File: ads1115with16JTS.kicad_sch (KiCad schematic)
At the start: 48 parts, among them J1 Conn_01x02_Pin, J10 Conn_01x02_Pin, J11 Conn_01x02_Pin, J12 Conn_01x02_Pin, J13 Conn_01x02_Pin, J14 Conn_01x02_Pin, J15 Conn_01x02_Pin, J16 Conn_01x02_Pin, J17 Conn_01x04_Pin, J18 PinSocket_1x20_P2.54mm_Vertic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, J19 PinSocket_1x20_P2.54mm_Vertic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, J2 Conn_01x02_Pin, J3 Conn_01x02_Pin, J4 Conn_01x02_Pin, J5 Conn_01x02_Pin, J6 Conn_01x02_Pin, J7 Conn_01x02_Pin, J8 Conn_01x02_Pin, J9 Conn_01x02_Pin, U1 ADS1115IDGS, U2 ADS1115IDGS, U3 ADS1115IDGS, U4 ADS1115IDGS

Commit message: snapshot v0.1.0-pre
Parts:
- removed pads1: SolderWire-0.25sqmm_1x04_P4.2mm_D0.65mm_OD1.7mm, SolderWire-0.25sqmm_1x04_P4.2mm_D0.65mm_OD1.7mm, symbol Connector:Conn_01x04_Pin
- added J20: Screw_Terminal_01x02, TerminalBlock_Phoenix:TerminalBlock_Phoenix_MPT-0,5-2-2.54_1x02_P2.54mm_Horizontal, symbol Connector:Screw_Terminal_01x02
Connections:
- net +3V3: now also J20.2 (Pin_2)
- net GND: now also J20.1 (Pin_1)
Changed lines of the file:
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@@
   (junction (at 125.73 171.45) (diameter 0) (color 0 0 0 0)
   )
-  (junction (at 184.15 53.34) (diameter 0) (color 0 0 0 0)
-  )
   (junction (at 125.73 142.24) (diameter 0) (color 0 0 0 0)
   )
@@
   (junction (at 186.69 105.41) (diameter 0) (color 0 0 0 0)
   )
-  (junction (at 186.69 50.8) (diameter 0) (color 0 0 0 0)
-  )
   (junction (at 143.51 69.85) (diameter 0) (color 0 0 0 0)
   )
-  (junction (at 193.04 58.42) (diameter 0) (color 0 0 0 0)
-  )
   (junction (at 190.5 113.03) (diameter 0) (color 0 0 0 0)
   )
@@
   (junction (at 48.26 184.15) (diameter 0) (color 0 0 0 0)
   )
-  (junction (at 190.5 55.88) (diameter 0) (color 0 0 0 0)
+  (junction (at 186.69 78.74) (diameter 0) (color 0 0 0 0)
   )
   (junction (at 162.56 148.59) (diameter 0) (color 0 0 0 0)
@@
   )
   (junction (at 189.23 110.49) (diameter 0) (color 0 0 0 0)
+  )
+  (junction (at 184.15 81.28) (diameter 0) (color 0 0 0 0)
   )
   (junction (at 49.53 250.19) (diameter 0) (color 0 0 0 0)
@@
     (stroke (width 0) (type default))
   )
-  (wire (pts (xy 189.23 55.88) (xy 190.5 55.88))
+  (wire (pts (xy 189.23 55.88) (xy 194.31 55.88))
     (stroke (width 0) (type default))
   )
@@
     (stroke (width 0) (type default))
   )
-  (wire (pts (xy 190.5 55.88) (xy 194.31 55.88))
-    (stroke (width 0) (type default))
-  )
   (wire (pts (xy 182.88 148.59) (xy 191.77 148.59))
     (stroke (width 0) (type default))
@@
     (stroke (width 0) (type default))
   )
+  (wire (pts (xy 186.69 78.74) (xy 186.69 62.23))
+    (stroke (width 0) (type default))
+  )
   (wire (pts (xy 140.97 218.44) (xy 138.43 218.44))
     (stroke (width 0) (type default))
@@
     (stroke (width 0) (type default))
   )
-  (wire (pts (xy 193.04 58.42) (xy 194.31 58.42))
+  (wire (pts (xy 190.5 58.42) (xy 194.31 58.42))
     (stroke (width 0) (type default))
   )
@@
     (stroke (width 0) (type default))
   )
-  (wire (pts (xy 190.5 38.1) (xy 190.5 55.88))
-    (stroke (width 0) (type default))
-  )
   (wire (pts (xy 182.88 123.19) (xy 191.77 123.19))
     (stroke (width 0) (type default))
@@
     (stroke (width 0) (type default))
   )
-  (wire (pts (xy 193.04 40.64) (xy 193.04 58.42))
-    (stroke (width 0) (type default))
-  )
   (wire (pts (xy 105.41 45.72) (xy 115.57 45.72))
     (stroke (width 0) (type default))
@@
     (stroke (width 0) (type default))
   )
+  (wire (pts (xy 184.15 81.28) (xy 184.15 64.77))
+    (stroke (width 0) (type default))
+  )
   (wire (pts (xy 186.69 50.8) (xy 194.31 50.8))
     (stroke (width 0) (type default))
   )
-  (wire (pts (xy 184.15 35.56) (xy 184.15 53.34))
-    (stroke (width 0) (type default))
-  )
   (wire (pts (xy 182.88 113.03) (xy 190.5 113.03))
     (stroke (width 0) (type default))
@@
     (stroke (width 0) (type default))
   )
+  (wire (pts (xy 175.26 78.74) (xy 186.69 78.74))
+    (stroke (width 0) (type default))
+  )
   (wire (pts (xy 78.74 148.59) (xy 115.57 148.59))
     (stroke (width 0) (type default))
@@
     (stroke (width 0) (type default))
   )
-  (wire (pts (xy 184.15 102.87) (xy 184.15 64.77))
+  (wire (pts (xy 184.15 102.87) (xy 184.15 81.28))
     (stroke (width 0) (type default))
   )
@@
     (stroke (width 0) (type default))
   )
-  (wire (pts (xy 190.5 58.42) (xy 193.04 58.42))
-    (stroke (width 0) (type default))
-  )
   (wire (pts (xy 157.48 120.65) (xy 162.56 120.65))
     (stroke (width 0) (type default))
@@
     (stroke (width 0) (type default))
   )
+  (wire (pts (xy 175.26 81.28) (xy 184.15 81.28))
+    (stroke (width 0) (type default))
+  )
   (wire (pts (xy 143.51 69.85) (xy 143.51 104.14))
     (stroke (width 0) (type default))
@@
     (stroke (width 0) (type default))
   )
-  (wire (pts (xy 193.04 38.1) (xy 190.5 38.1))
-    (stroke (width 0) (type default))
-  )
   (wire (pts (xy 157.48 151.13) (xy 162.56 151.13))
     (stroke (width 0) (type default))
@@
     (stroke (width 0) (type default))
   )
-  (wire (pts (xy 186.69 33.02) (xy 186.69 50.8))
-    (stroke (width 0) (type default))
-  )
   (wire (pts (xy 182.88 140.97) (xy 191.77 140.97))
     (stroke (width 0) (type default))
@@
     (stroke (width 0) (type default))
   )
-  (wire (pts (xy 193.04 33.02) (xy 186.69 33.02))
-    (stroke (width 0) (type default))
-  )
   (wire (pts (xy 160.02 64.77) (xy 167.64 64.77))
     (stroke (width 0) (type default))
@@
     (stroke (width 0) (type default))
   )
-  (wire (pts (xy 193.04 35.56) (xy 184.15 35.56))
-    (stroke (width 0) (type default))
-  )
-  (wire (pts (xy 186.69 105.41) (xy 186.69 62.23))
+  (wire (pts (xy 186.69 105.41) (xy 186.69 78.74))
     (stroke (width 0) (type default))
   )
@@
     )
   )
-  (symbol (lib_id "Connector:Conn_01x04_Pin") (at 198.12 35.56 0) (mirror y) (unit 1)
-    (in_bom yes) (on_board yes) (dnp no)
-    (property "Reference" "pads1" (at 197.485 27.94 0)
-      (effects (font (size 1.27 1.27)))
-    )
-    (property "Value" "SolderWire-0.25sqmm_1x04_P4.2mm_D0.65mm_OD1.7mm\n" (at 197.485 30.48 0)
-      (effects (font (size 1.27 1.27)))
-    )
-    (property "Footprint" "SolderWire-0.25sqmm_1x04_P4.2mm_D0.65mm_OD1.7mm" (at 198.12 35.56 0)
-      (effects (font (size 1.27 1.27)) hide)
-    )
-    (property "Datasheet" "~" (at 198.12 35.56 0)
-      (effects (font (size 1.27 1.27)) hide)
-    )
-    (pin "1")
-    (pin "2")
-    (pin "3")
-    (pin "4")
-    (instances
-      (project "ads1115with16JTS"
-        (path "/0c2d0c14-8850-4a30-bb78-b2f40cb442ba"
-          (reference "pads1") (unit 1)
-        )
-      )
-    )
-  )
   (symbol (lib_id "power:+3V3") (at 48.26 31.75 0) (unit 1)
     (in_bom yes) (on_board yes) (dnp no)
@@
         )
       )
+    )
+  )
+  (symbol (lib_id "Connector:Screw_Terminal_01x02") (at 170.18 78.74 0) (mirror y) (unit 1)
+    (in_bom yes) (on_board yes) (dnp no)
+    (property "Reference" "J20" (at 167.64 78.74 0)
+      (effects (font (size 1.27 1.27)) (justify left))
+    )
+    (property "Value" "Screw_Terminal_01x02" (at 167.64 81.28 0)
+      (effects (font (size 1.27 1.27)) (justify left))
+    )
+    (property "Footprint" "TerminalBlock_Phoenix:TerminalBlock_Phoenix_MPT-0,5-2-2.54_1x02_P2.54mm_Horizontal" (at 170.18 78.74 0)
+      (effects (font (size 1.27 1.27)) hide)
+    )
+    (property "Datasheet" "~" (at 170.18 78.74 0)
+      (effects (font (size 1.27 1.27)) hide)
+    )
+    (pin "1")
+    (pin "2")
+    (instances
+      (project "ads1115with16JTS"
+        (path "/0c2d0c14-8850-4a30-bb78-b2f40cb442ba"
+          (reference "J20") (unit 1)
+        )
+      )

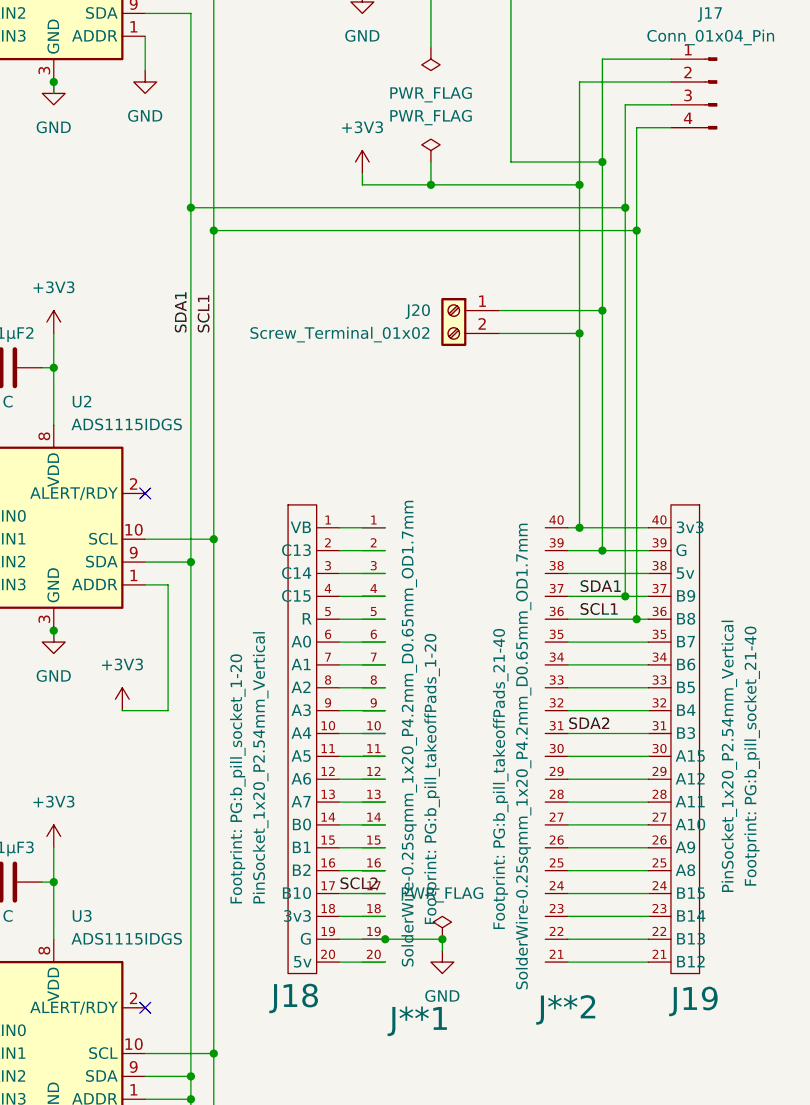
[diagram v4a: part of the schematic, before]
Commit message: change solder mask for takeoff pads, which will not be soldered.
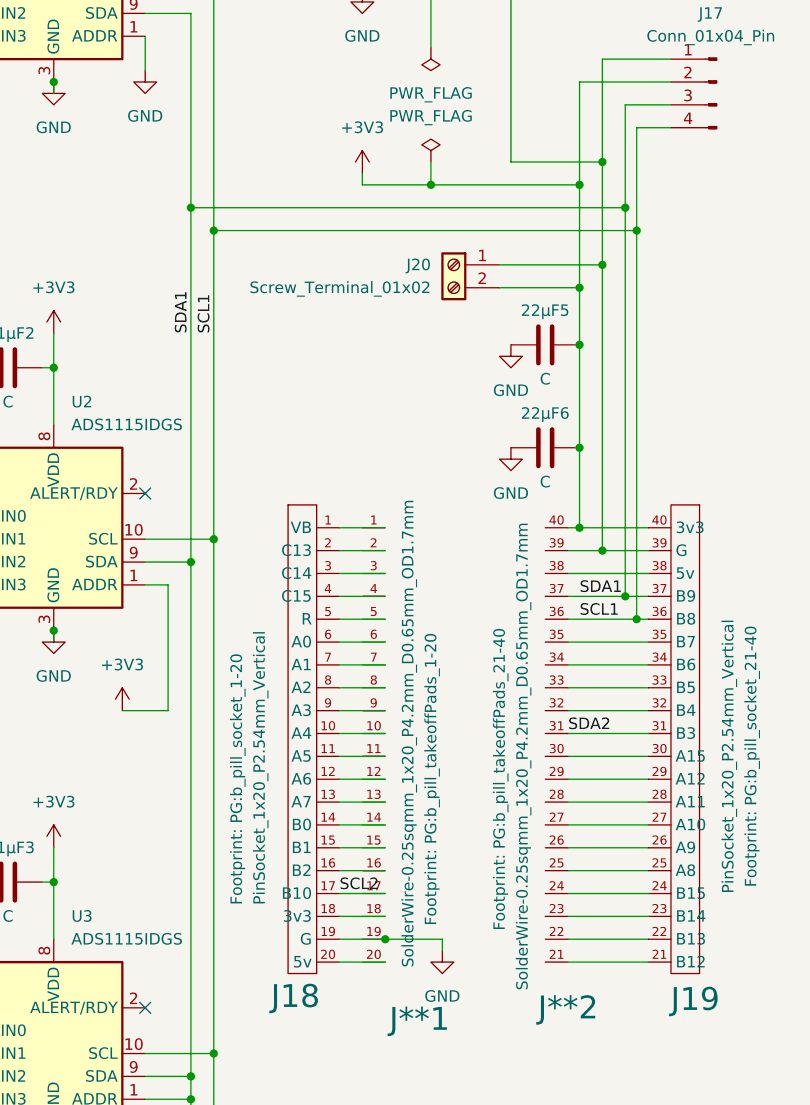
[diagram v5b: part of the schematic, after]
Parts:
- added 22µF5, 22µF6: C, Capacitor_SMD:C_0805_2012Metric, symbol Device:C
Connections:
- net +3V3: now also 22µF5.1, 22µF6.1
- net GND: now also 22µF5.2, 22µF6.2
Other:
- moved on the sheet: J20
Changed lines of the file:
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@@
   (junction (at 184.15 102.87) (diameter 0) (color 0 0 0 0)
   )
+  (junction (at 186.69 73.66) (diameter 0) (color 0 0 0 0)
+  )
   (junction (at 140.97 166.37) (diameter 0) (color 0 0 0 0)
   )
@@
   (junction (at 140.97 67.31) (diameter 0) (color 0 0 0 0)
   )
-  (junction (at 168.91 148.59) (diameter 0) (color 0 0 0 0)
-  )
   (junction (at 125.73 171.45) (diameter 0) (color 0 0 0 0)
   )
@@
   (junction (at 143.51 69.85) (diameter 0) (color 0 0 0 0)
   )
+  (junction (at 184.15 93.98) (diameter 0) (color 0 0 0 0)
+  )
+  (junction (at 184.15 76.2) (diameter 0) (color 0 0 0 0)
+  )
   (junction (at 190.5 113.03) (diameter 0) (color 0 0 0 0)
   )
@@
   (junction (at 48.26 184.15) (diameter 0) (color 0 0 0 0)
   )
-  (junction (at 186.69 78.74) (diameter 0) (color 0 0 0 0)
-  )
   (junction (at 162.56 148.59) (diameter 0) (color 0 0 0 0)
   )
@@
   (junction (at 189.23 110.49) (diameter 0) (color 0 0 0 0)
   )
-  (junction (at 184.15 81.28) (diameter 0) (color 0 0 0 0)
-  )
   (junction (at 49.53 250.19) (diameter 0) (color 0 0 0 0)
   )
@@
   )
   (junction (at 48.26 157.48) (diameter 0) (color 0 0 0 0)
+  )
+  (junction (at 184.15 82.55) (diameter 0) (color 0 0 0 0)
   )
   (junction (at 48.26 39.37) (diameter 0) (color 0 0 0 0)
@@
     (stroke (width 0) (type default))
   )
+  (wire (pts (xy 184.15 76.2) (xy 184.15 64.77))
+    (stroke (width 0) (type default))
+  )
   (wire (pts (xy 162.56 148.59) (xy 168.91 148.59))
     (stroke (width 0) (type default))
@@
     (stroke (width 0) (type default))
   )
+  (wire (pts (xy 184.15 76.2) (xy 184.15 82.55))
+    (stroke (width 0) (type default))
+  )
   (wire (pts (xy 157.48 133.35) (xy 162.56 133.35))
     (stroke (width 0) (type default))
@@
     (stroke (width 0) (type default))
   )
+  (wire (pts (xy 186.69 73.66) (xy 186.69 62.23))
+    (stroke (width 0) (type default))
+  )
   (wire (pts (xy 186.69 105.41) (xy 191.77 105.41))
     (stroke (width 0) (type default))
@@
     (stroke (width 0) (type default))
   )
-  (wire (pts (xy 186.69 78.74) (xy 186.69 62.23))
-    (stroke (width 0) (type default))
-  )
   (wire (pts (xy 140.97 218.44) (xy 138.43 218.44))
     (stroke (width 0) (type default))
@@
     (stroke (width 0) (type default))
   )
-  (wire (pts (xy 184.15 81.28) (xy 184.15 64.77))
-    (stroke (width 0) (type default))
-  )
   (wire (pts (xy 186.69 50.8) (xy 194.31 50.8))
     (stroke (width 0) (type default))
@@
     (stroke (width 0) (type default))
   )
-  (wire (pts (xy 175.26 78.74) (xy 186.69 78.74))
+  (wire (pts (xy 175.26 73.66) (xy 186.69 73.66))
     (stroke (width 0) (type default))
   )
@@
     (stroke (width 0) (type default))
   )
-  (wire (pts (xy 184.15 102.87) (xy 184.15 81.28))
+  (wire (pts (xy 184.15 93.98) (xy 184.15 102.87))
     (stroke (width 0) (type default))
   )
@@
     (stroke (width 0) (type default))
   )
+  (wire (pts (xy 184.15 82.55) (xy 184.15 93.98))
+    (stroke (width 0) (type default))
+  )
   (wire (pts (xy 157.48 105.41) (xy 162.56 105.41))
     (stroke (width 0) (type default))
@@
     (stroke (width 0) (type default))
   )
-  (wire (pts (xy 175.26 81.28) (xy 184.15 81.28))
+  (wire (pts (xy 175.26 76.2) (xy 184.15 76.2))
     (stroke (width 0) (type default))
   )
@@
     (stroke (width 0) (type default))
   )
-  (wire (pts (xy 186.69 105.41) (xy 186.69 78.74))
-    (stroke (width 0) (type default))
-  )
   (wire (pts (xy 109.22 115.57) (xy 109.22 106.68))
     (stroke (width 0) (type default))
@@
   )
   (wire (pts (xy 189.23 110.49) (xy 191.77 110.49))
+    (stroke (width 0) (type default))
+  )
+  (wire (pts (xy 186.69 73.66) (xy 186.69 105.41))
     (stroke (width 0) (type default))
   )
@@
     )
   )
-  (symbol (lib_id "power:PWR_FLAG") (at 168.91 148.59 0) (unit 1)
-    (in_bom yes) (on_board yes) (dnp no) (fields_autoplaced)
-    (property "Reference" "#FLG03" (at 168.91 146.685 0)
-      (effects (font (size 1.27 1.27)) hide)
-    )
-    (property "Value" "PWR_FLAG" (at 168.91 143.51 0)
-      (effects (font (size 1.27 1.27)))
-    )
-    (property "Footprint" "" (at 168.91 148.59 0)
-      (effects (font (size 1.27 1.27)) hide)
-    )
-    (property "Datasheet" "~" (at 168.91 148.59 0)
-      (effects (font (size 1.27 1.27)) hide)
-    )
-    (pin "1")
-    (instances
-      (project "ads1115with16JTS"
-        (path "/0c2d0c14-8850-4a30-bb78-b2f40cb442ba"
-          (reference "#FLG03") (unit 1)
-        )
-      )
-    )
-  )
   (symbol (lib_id "Connector:Conn_01x02_Pin") (at 43.18 184.15 0) (unit 1)
     (in_bom yes) (on_board yes) (dnp no)
@@
     )
   )
+  (symbol (lib_id "Device:C") (at 180.34 93.98 270) (mirror x) (unit 1)
+    (in_bom yes) (on_board yes) (dnp no)
+    (property "Reference" "22µF6" (at 180.34 90.17 90)
+      (effects (font (size 1.27 1.27)))
+    )
+    (property "Value" "C" (at 180.34 97.79 90)
+      (effects (font (size 1.27 1.27)))
+    )
+    (property "Footprint" "Capacitor_SMD:C_0805_2012Metric" (at 176.53 93.0148 0)
+      (effects (font (size 1.27 1.27)) hide)
+    )
+    (property "Datasheet" "~" (at 180.34 93.98 0)
+      (effects (font (size 1.27 1.27)) hide)
+    )
+    (pin "1")
+    (pin "2")
+    (instances
+      (project "ads1115with16JTS"
+        (path "/0c2d0c14-8850-4a30-bb78-b2f40cb442ba"
+          (reference "22µF6") (unit 1)
+        )
+      )
+    )
+  )
   (symbol (lib_id "power:GND") (at 125.73 114.3 0) (unit 1)
     (in_bom yes) (on_board yes) (dnp no) (fields_autoplaced)
@@
         (path "/0c2d0c14-8850-4a30-bb78-b2f40cb442ba"
           (reference "J9") (unit 1)
+        )
+      )
+    )
+  )
+  (symbol (lib_id "power:GND") (at 176.53 82.55 0) (unit 1)
+    (in_bom yes) (on_board yes) (dnp no) (fields_autoplaced)
+    (property "Reference" "#PWR050" (at 176.53 88.9 0)
+      (effects (font (size 1.27 1.27)) hide)
+    )
+    (property "Value" "GND" (at 176.53 87.63 0)
+      (effects (font (size 1.27 1.27)))
+    )
+    (property "Footprint" "" (at 176.53 82.55 0)
+      (effects (font (size 1.27 1.27)) hide)
+    )
+    (property "Datasheet" "" (at 176.53 82.55 0)
+      (effects (font (size 1.27 1.27)) hide)
+    )
+    (pin "1")
+    (instances
+      (project "ads1115with16JTS"
+        (path "/0c2d0c14-8850-4a30-bb78-b2f40cb442ba"
+          (reference "#PWR050") (unit 1)
         )
       )
@@
     )
   )
+  (symbol (lib_id "Device:C") (at 180.34 82.55 270) (mirror x) (unit 1)
+    (in_bom yes) (on_board yes) (dnp no)
+    (property "Reference" "22µF5" (at 180.34 78.74 90)
+      (effects (font (size 1.27 1.27)))
+    )
+    (property "Value" "C" (at 180.34 86.36 90)
+      (effects (font (size 1.27 1.27)))
+    )
+    (property "Footprint" "Capacitor_SMD:C_0805_2012Metric" (at 176.53 81.5848 0)
+      (effects (font (size 1.27 1.27)) hide)
+    )
+    (property "Datasheet" "~" (at 180.34 82.55 0)
+      (effects (font (size 1.27 1.27)) hide)
+    )
+    (pin "1")
+    (pin "2")
+    (instances
+      (project "ads1115with16JTS"
+        (path "/0c2d0c14-8850-4a30-bb78-b2f40cb442ba"
+          (reference "22µF5") (unit 1)
+        )
+      )
+    )
+  )
   (symbol (lib_id "power:+3V3") (at 78.74 81.28 0) (unit 1)
     (in_bom yes) (on_board yes) (dnp no)
@@
         (path "/0c2d0c14-8850-4a30-bb78-b2f40cb442ba"
           (reference "#PWR02") (unit 1)
+        )
+      )
+    )
+  )
+  (symbol (lib_id "power:GND") (at 176.53 93.98 0) (unit 1)
+    (in_bom yes) (on_board yes) (dnp no) (fields_autoplaced)
+    (property "Reference" "#PWR051" (at 176.53 100.33 0)
+      (effects (font (size 1.27 1.27)) hide)
+    )
+    (property "Value" "GND" (at 176.53 99.06 0)
+      (effects (font (size 1.27 1.27)))
+    )
+    (property "Footprint" "" (at 176.53 93.98 0)
+      (effects (font (size 1.27 1.27)) hide)
+    )
+    (property "Datasheet" "" (at 176.53 93.98 0)
+      (effects (font (size 1.27 1.27)) hide)
+    )
+    (pin "1")
+    (instances
+      (project "ads1115with16JTS"
+        (path "/0c2d0c14-8850-4a30-bb78-b2f40cb442ba"
+          (reference "#PWR051") (unit 1)
         )
       )
@@
     )
   )
-  (symbol (lib_id "Connector:Screw_Terminal_01x02") (at 170.18 78.74 0) (mirror y) (unit 1)
+  (symbol (lib_id "Connector:Screw_Terminal_01x02") (at 170.18 73.66 0) (mirror y) (unit 1)
     (in_bom yes) (on_board yes) (dnp no)
-    (property "Reference" "J20" (at 167.64 78.74 0)
-      (effects (font (size 1.27 1.27)) (justify left))
-    )
-    (property "Value" "Screw_Terminal_01x02" (at 167.64 81.28 0)
-      (effects (font (size 1.27 1.27)) (justify left))
-    )
-    (property "Footprint" "TerminalBlock_Phoenix:TerminalBlock_Phoenix_MPT-0,5-2-2.54_1x02_P2.54mm_Horizontal" (at 170.18 78.74 0)
-      (effects (font (size 1.27 1.27)) hide)
-    )
-    (property "Datasheet" "~" (at 170.18 78.74 0)
-      (effects (font (size 1.27 1.27)) hide)
-    )
+    (property "Reference" "J20" (at 167.64 73.66 0)
+      (effects (font (size 1.27 1.27)) (justify left))
+    )
+    (property "Value" "Screw_Terminal_01x02" (at 167.64 76.2 0)
+      (effects (font (size 1.27 1.27)) (justify left))
+    )
+    (property "Footprint" "TerminalBlock_Phoenix:TerminalBlock_Phoenix_MPT-0,5-2-2.54_1x02_P2.54mm_Horizontal" (at 170.18 73.66 0)
+      (effects (font (size 1.27 1.27)) hide)
+    )
+    (property "Datasheet" "~" (at 170.18 73.66 0)
+      (effects (font (size 1.27 1.27)) hide)
+    )

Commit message: moved PG.kicad_sym to ProjectLib.kicad_sym and added all project symbols so project has a complete set of stable symbols.
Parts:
- 0.1µF1, 0.1µF2, 0.1µF3, 0.1µF4, 22µF5, 22µF6: symbol Device:C -> ProjectLib:C
- H1, H2: symbol Mechanical:MountingHole -> ProjectLib:MountingHole
- J**1: symbol PG:b_pill_takeoff_1-20 -> ProjectLib:b_pill_takeoff_1-20
- J**2: symbol PG:b_pill_takeoff_21-40 -> ProjectLib:b_pill_takeoff_21-40
- J1, J10, J11, J12, J13, J14, J15, J16, J2, J3, J4, J5, J6, J7, J8, J9: symbol Connector:Conn_01x02_Pin -> ProjectLib:Conn_01x02_Pin
- J17: symbol Connector:Conn_01x04_Pin -> ProjectLib:Conn_01x04_Pin
- J18: symbol PG:b_pill_1-20 -> ProjectLib:b_pill_1-20
- J19: symbol PG:b_pill_21-40 -> ProjectLib:b_pill_21-40
- J20: symbol Connector:Screw_Terminal_01x02 -> ProjectLib:Screw_Terminal_01x02
- R1, R10, R11, R12, R13, R14, R15, R16, R2, R3, R4, R5, R6, R7, R8, R9: symbol Device:R_US -> ProjectLib:R_US
- U1, U2, U3, U4: symbol Analog_ADC:ADS1115IDGS -> ProjectLib:ADS1115IDGS
